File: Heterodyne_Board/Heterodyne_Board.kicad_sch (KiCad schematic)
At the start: 47 parts, among them J1 AVR-ISP-6, J2 Speaker, SW1 SW_SPST, U1 ATtiny85-20P, U2 TLV9054xD, U3 AP2112K-3.3, U4 LM386, U5 W25X40CLSN, U6 TLV9054xD, U7 TLV9054xD

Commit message: Schematic dun dun DUN
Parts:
- removed D2, D3, D4: D_Schottky, symbol Device:D_Schottky
- removed SW1: SW_SPST, symbol Switch:SW_SPST
- removed unit 2 of U6
- added D2, D3, D4: MBR0520, Diode_SMD:D_SOD-123, symbol Diode:MBR0520
- added J3: SWITCH, Connector_Molex:Molex_KK-254_AE-6410-02A_1x02_P2.54mm_Vertical, symbol Connector_Generic:Conn_01x02
- added TP1, TP3: TestPoint, TestPoint:TestPoint_Pad_1.0x1.0mm, symbol Connector:TestPoint
- added unit 2 of U2
- C1, C10, C14, C2, C3, C4, C6: footprint (none) -> Capacitor_SMD:C_0805_2012Metric_Pad1.18x1.45mm_HandSolder
- C11: footprint (none) -> Capacitor_SMD:C_1206_3216Metric_Pad1.33x1.80mm_HandSolder
- C5: value 7n -> 4.7n; footprint (none) -> Capacitor_SMD:C_1206_3216Metric_Pad1.33x1.80mm_HandSolder
- C7: value 250u -> 220u; footprint (none) -> Capacitor_SMD:C_0805_2012Metric_Pad1.18x1.45mm_HandSolder
- C8, C9: value 50n -> 47n; footprint (none) -> Capacitor_SMD:C_0805_2012Metric_Pad1.18x1.45mm_HandSolder
- D1: footprint (none) -> LED_SMD:LED_0805_2012Metric_Pad1.15x1.40mm_HandSolder
- J1: footprint (none) -> Connector_IDC:IDC-Header_2x03_P2.54mm_Vertical
- J2: footprint (none) -> Connector_Molex:Molex_KK-254_AE-6410-02A_1x02_P2.54mm_Vertical
- MK1: footprint (none) -> Sensor_Audio:Knowles_LGA-5_3.5x2.65mm
- R1, R10, R11, R12, R13, R14, R15, R16, R2, R3, R6, R7, R8, R9: footprint (none) -> Resistor_SMD:R_0805_2012Metric_Pad1.20x1.40mm_HandSolder
- R4: value 3k -> 3.16k; footprint (none) -> Resistor_SMD:R_0805_2012Metric_Pad1.20x1.40mm_HandSolder
- R5: value 30k -> 33k; footprint (none) -> Resistor_SMD:R_0805_2012Metric_Pad1.20x1.40mm_HandSolder
- RV1: footprint (none) -> Potentiometer_SMD:Potentiometer_Bourns_3269W_Vertical
- RV3: value 10k -> R_Potentiometer; footprint (none) -> Potentiometer_THT:Potentiometer_Bourns_PTV09A-1_Single_Vertical
- RV4: footprint (none) -> Potentiometer_THT:Potentiometer_Bourns_PTV09A-1_Single_Vertical
- TP2: footprint (none) -> TestPoint:TestPoint_Pad_1.0x1.0mm
- U4: footprint (none) -> Package_DIP:DIP-8_W7.62mm
- renumbered U7 to U2, U6 to U2
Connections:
- net +3V3: now also D2.1 (K)
- net +5V: now also D4.2 (A)
- net +6V: now also J3.1 (Pin_1)
- net Osci_out: now also TP1.1
- net RESET: now also J1.5 (~{RST}), R1.2
- net Speaker_in: now also TP3.1
- net at R10.2, R11.1, R9.2: now also D2.2 (A)
- net at J1.2 (VCC): now also D4.1 (K)
- net at C1.1, U3.1 (VIN), U3.3 (EN): now also D3.1 (K)
- new net: D3.2 (A), J3.2 (Pin_2)
- no-connect marks 2 -> 5

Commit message: continued PCB design
modules organized except for audio amp, no wiring yet
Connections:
- net at RV4.2: now also R8.2
- net at RV4.3: no longer R8.2
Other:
- moved on the sheet: RV4
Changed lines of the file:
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@@
+	)
+	(junction
+		(at 134.62 170.18)
+		(diameter 0)
+		(color 0 0 0 0)
 	)
 	(junction
@@
 	)
 	(junction
-		(at 134.62 170.18)
-		(diameter 0)
-		(color 0 0 0 0)
-	)
-	(junction
 		(at 105.41 167.64)
 		(diameter 0)
@@
 	)
 	(no_connect
-		(at 219.71 105.41)
+		(at 219.71 113.03)
 	)
 	(no_connect
@@
 	(wire
 		(pts
+			(xy 219.71 104.14) (xy 219.71 105.41)
+		)
+		(stroke
+			(width 0)
+			(type default)
+		)
+	)
+	(wire
+		(pts
 			(xy 196.85 110.49) (xy 196.85 121.92)
 		)
@@
 	(wire
 		(pts
-			(xy 210.82 109.22) (xy 215.9 109.22)
-		)
-		(stroke
-			(width 0)
-			(type default)
-		)
-	)
-	(wire
-		(pts
 			(xy 48.26 113.03) (xy 48.26 115.57)
 		)
@@
 	(wire
 		(pts
+			(xy 210.82 104.14) (xy 210.82 109.22)
+		)
+		(stroke
+			(width 0)
+			(type default)
+		)
+	)
+	(wire
+		(pts
 			(xy 71.12 52.07) (xy 71.12 54.61)
 		)
@@
 		(pts
 			(xy 180.34 35.56) (xy 175.26 35.56)
+		)
+		(stroke
+			(width 0)
+			(type default)
+		)
+	)
+	(wire
+		(pts
+			(xy 219.71 104.14) (xy 210.82 104.14)
 		)
 		(stroke
@@
 	(symbol
 		(lib_id "Device:R_Potentiometer")
-		(at 219.71 109.22 90)
+		(at 219.71 109.22 0)
 		(unit 1)
 		(exclude_from_sim no)
@@
 		(dnp no)
 		(property "Reference" "RV4"
-			(at 219.71 99.822 90)
+			(at 229.616 102.87 0)
 			(effects
 				(font
@@
 		)
 		(property "Value" "R_Potentiometer"
-			(at 219.71 102.362 90)
-			(effects
-				(font
+			(at 229.616 105.41 0)
+			(effects
+				(font

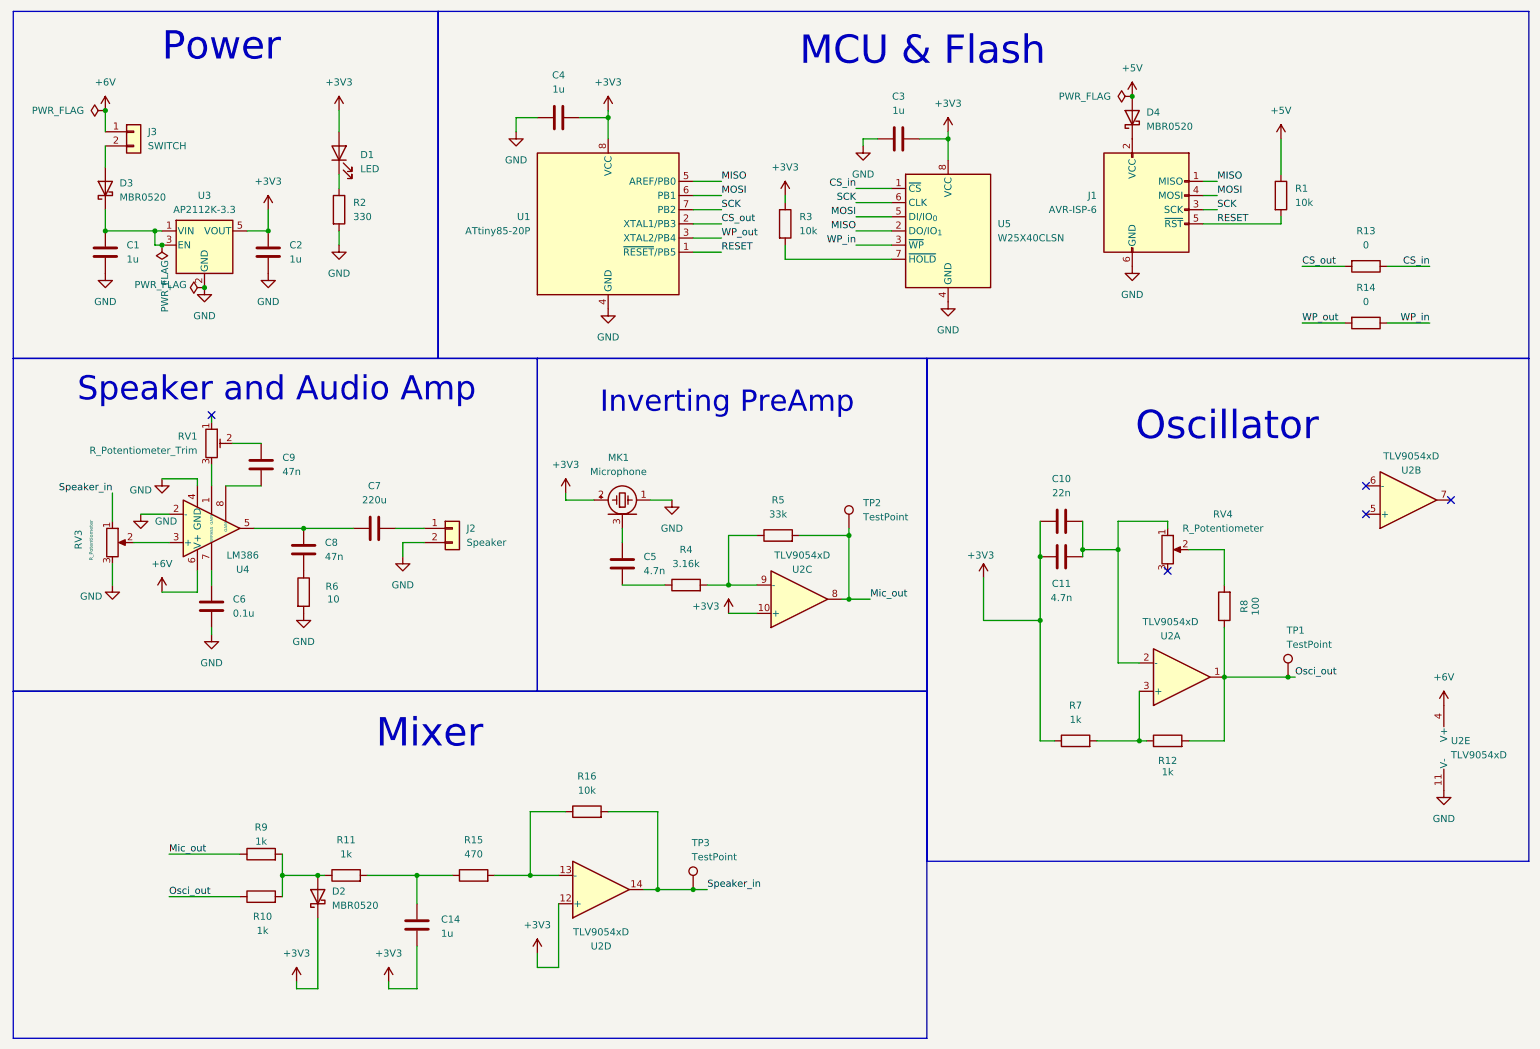
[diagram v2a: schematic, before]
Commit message: finished the basic PCB layout
no wiring has been done yet though
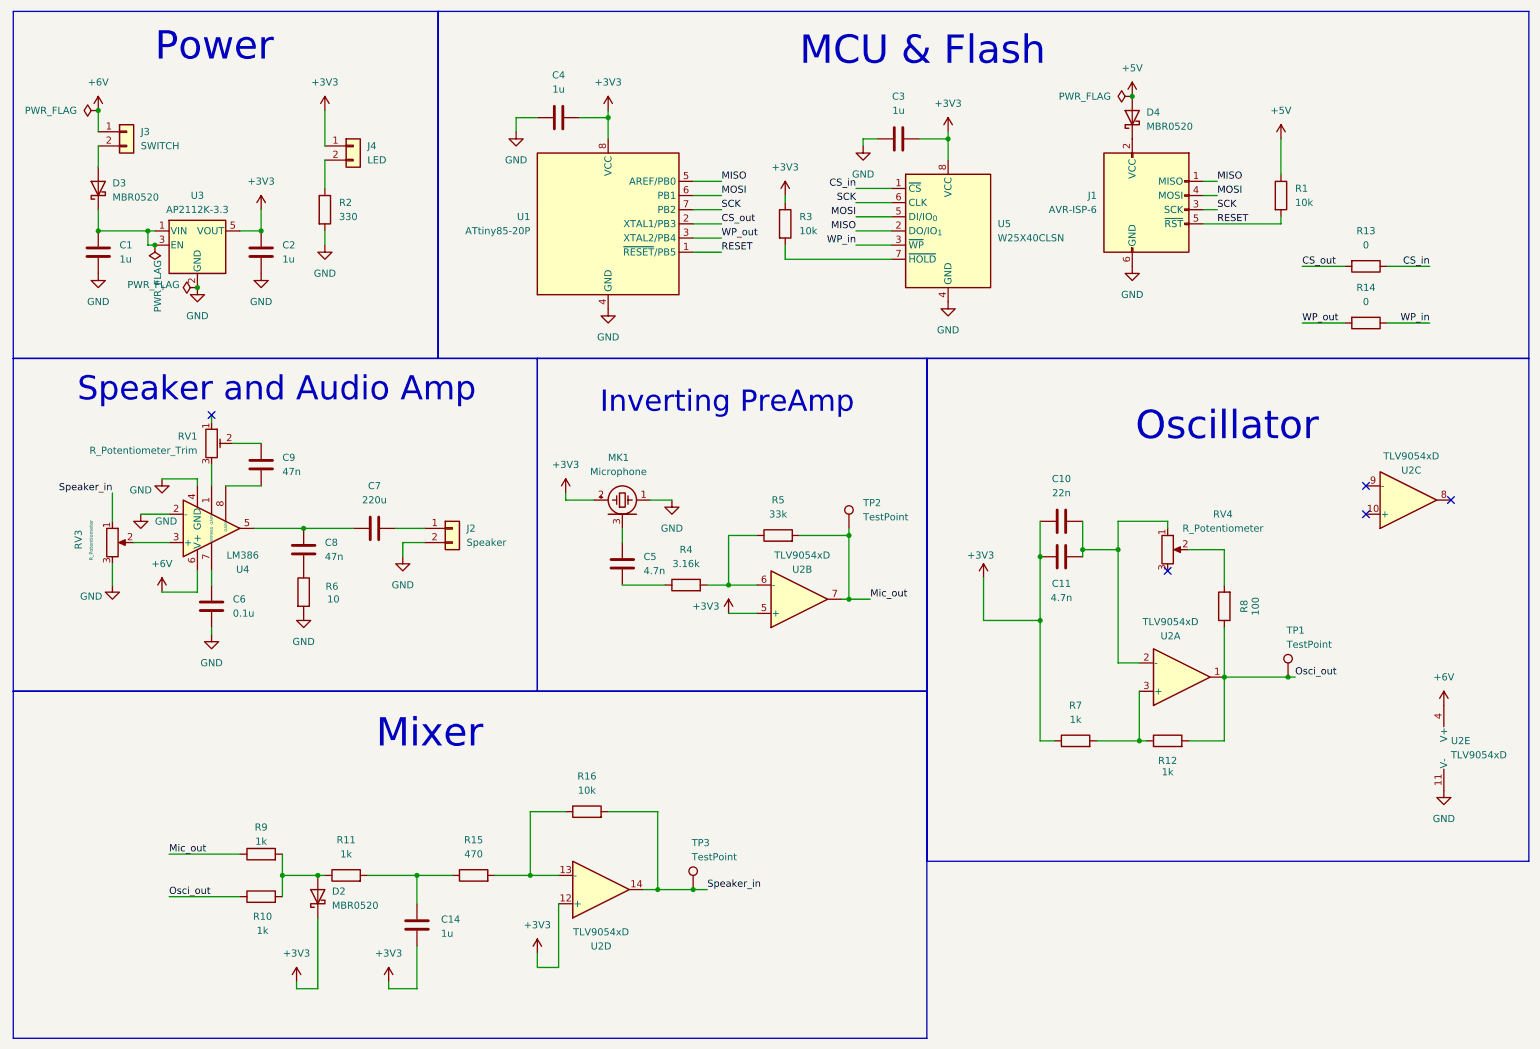
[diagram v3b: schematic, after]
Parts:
- removed D1: LED, LED_SMD:LED_0805_2012Metric_Pad1.15x1.40mm_HandSolder, symbol Device:LED
- added J4: LED, Connector_Molex:Molex_KK-254_AE-6410-02A_1x02_P2.54mm_Vertical, symbol Connector_Generic:Conn_01x02
- C11, C5: footprint Capacitor_SMD:C_1206_3216Metric_Pad1.33x1.80mm_HandSolder -> Capacitor_SMD:C_0805_2012Metric_Pad1.18x1.45mm_HandSolder
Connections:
- net +3V3: now also U2.5 (+), J4.1 (Pin_1); no longer U2.10 (+)
- net Mic_out: now also U2.7; no longer U2.8
- net at R2.1: now also J4.2 (Pin_2)
- net at U2.6 (-): now also R4.2, R5.1
- now unconnected: U2.9 (-)
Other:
- moved on the sheet: C1, C2, D3, J3, R2, U3

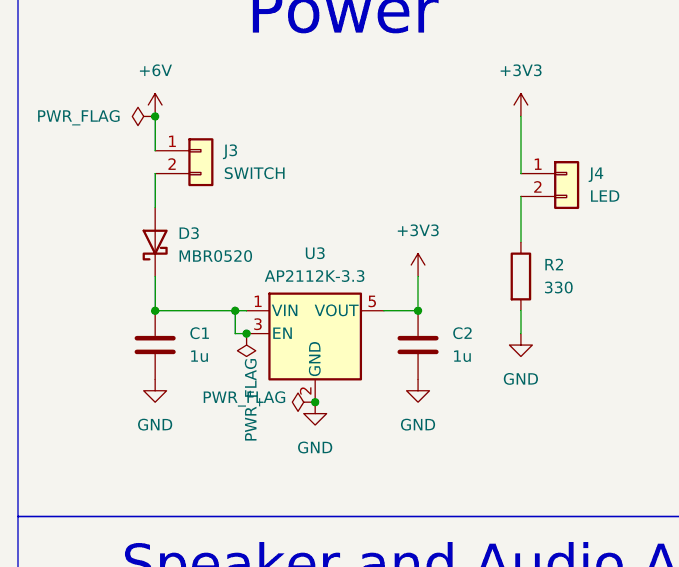
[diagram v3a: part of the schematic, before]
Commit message: added two new testpoints
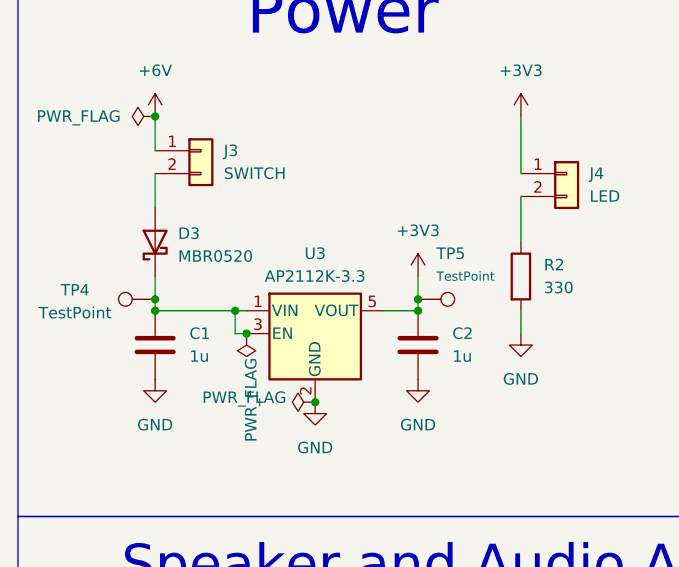
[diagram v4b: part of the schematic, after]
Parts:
- added TP4, TP5: TestPoint, TestPoint:TestPoint_Pad_1.0x1.0mm, symbol Connector:TestPoint
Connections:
- net +3V3: now also TP5.1
- net at C1.1, D3.1 (K), U3.1 (VIN)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: now also TP4.1
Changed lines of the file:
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@@
 	)
 	(junction
+		(at 57.15 50.8)
+		(diameter 0)
+		(color 0 0 0 0)
+	)
+	(junction
 		(at 45.72 62.23)
 		(diameter 0)
@@
 		(color 0 0 0 0)
 	)
+	(junction
+		(at 27.94 50.8)
+		(diameter 0)
+		(color 0 0 0 0)
+	)
 	(no_connect
 		(at 219.71 113.03)
@@
 	(wire
 		(pts
+			(xy 27.94 50.8) (xy 27.94 52.07)
+		)
+		(stroke
+			(width 0)
+			(type default)
+		)
+	)
+	(wire
+		(pts
 			(xy 163.83 54.61) (xy 170.18 54.61)
 		)
@@
 	(wire
 		(pts
-			(xy 57.15 48.26) (xy 57.15 52.07)
+			(xy 57.15 48.26) (xy 57.15 50.8)
 		)
 		(stroke
@@
 	(wire
 		(pts
-			(xy 27.94 48.26) (xy 27.94 52.07)
+			(xy 27.94 48.26) (xy 27.94 50.8)
 		)
 		(stroke
@@
 	(wire
 		(pts
+			(xy 57.15 50.8) (xy 57.15 52.07)
+		)
+		(stroke
+			(width 0)
+			(type default)
+		)
+	)
+	(wire
+		(pts
 			(xy 240.03 49.53) (xy 240.03 50.8)
 		)
@@
 	)
 	(symbol
+		(lib_id "Connector:TestPoint")
+		(at 57.15 50.8 270)
+		(unit 1)
+		(exclude_from_sim no)
+		(in_bom yes)
+		(on_board yes)
+		(dnp no)
+		(property "Reference" "TP5"
+			(at 59.182 45.72 90)
+			(effects
+				(font
+					(size 1.27 1.27)
+				)
+				(justify left)
+			)
+		)
+		(property "Value" "TestPoint"
+			(at 59.182 48.26 90)
+			(effects
+				(font
+					(size 1.016 1.016)
+				)
+				(justify left)
+			)
+		)
+		(property "Footprint" "TestPoint:TestPoint_Pad_1.0x1.0mm"
+			(at 57.15 55.88 0)
+			(effects
+				(font
+					(size 1.27 1.27)
+				)
+				(hide yes)
+			)
+		)
+		(property "Datasheet" "~"
+			(at 57.15 55.88 0)
+			(effects
+				(font
+					(size 1.27 1.27)
+				)
+				(hide yes)
+			)
+		)
+		(property "Description" "test point"
+			(at 57.15 50.8 0)
+			(effects
+				(font
+					(size 1.27 1.27)
+				)
+				(hide yes)
+			)
+		)
+		(pin "1"
+		)
+		(instances
+			(project "Heterodyne_Board"
+				(path "/bcb6d128-b2b2-45d9-80e5-2a1305aaf770"
+					(reference "TP5")
+					(unit 1)
+				)
+			)
+		)
+	)
+	(symbol
 		(lib_id "Device:R")
 		(at 133.35 115.57 90)
@@
 					(unit 1)
 				)
+			)
+		)
+	)
+	(symbol
+		(lib_id "Connector:TestPoint")
+		(at 27.94 50.8 90)
+		(unit 1)
+		(exclude_from_sim no)
+		(in_bom yes)
+		(on_board yes)
+		(dnp no)
+		(property "Reference" "TP4"
+			(at 19.05 49.784 90)
+			(effects
+				(font
+					(size 1.27 1.27)
+				)
+			)
+		)
+		(property "Value" "TestPoint"
+			(at 19.05 52.324 90)
+			(effects
+				(font
+					(size 1.27 1.27)
+				)
+			)
+		)
+		(property "Footprint" "TestPoint:TestPoint_Pad_1.0x1.0mm"
+			(at 27.94 45.72 0)
+			(effects
+				(font
+					(size 1.27 1.27)
+				)
+				(hide yes)
+			)
+		)
+		(property "Datasheet" "~"
+			(at 27.94 45.72 0)
+			(effects
+				(font
+					(size 1.27 1.27)
+				)
+				(hide yes)
+			)
+		)
+		(property "Description" "test point"
+			(at 27.94 50.8 0)
+			(effects
+				(font
+					(size 1.27 1.27)
+				)
+				(hide yes)
+			)
+		)
+		(pin "1"
+		)
+		(instances
+			(project "Heterodyne_Board"
+				(path "/bcb6d128-b2b2-45d9-80e5-2a1305aaf770"
+					(reference "TP4")
+					(unit 1)
+				)
